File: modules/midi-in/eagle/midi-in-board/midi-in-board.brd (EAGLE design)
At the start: 101.6 x 63.5 mm, 28 parts, among them IC1 LM358N, X1 POWER IN, X2 MIDI IN, X3 MIDI THRU, X4 CHANNEL SELECT SW, X5 22-23-2051, X6 POWER OUT CV

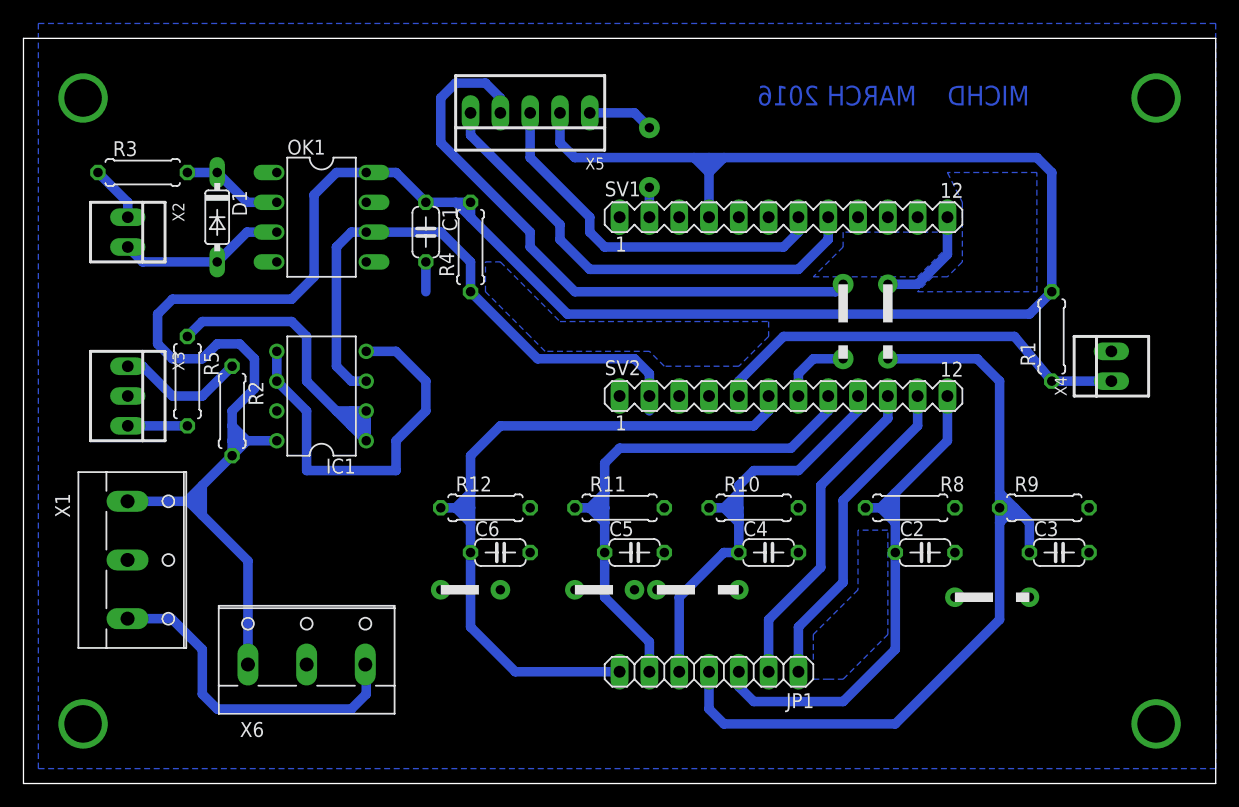
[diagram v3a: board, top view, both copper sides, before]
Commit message: Resize boards to be 10cm wide exactly
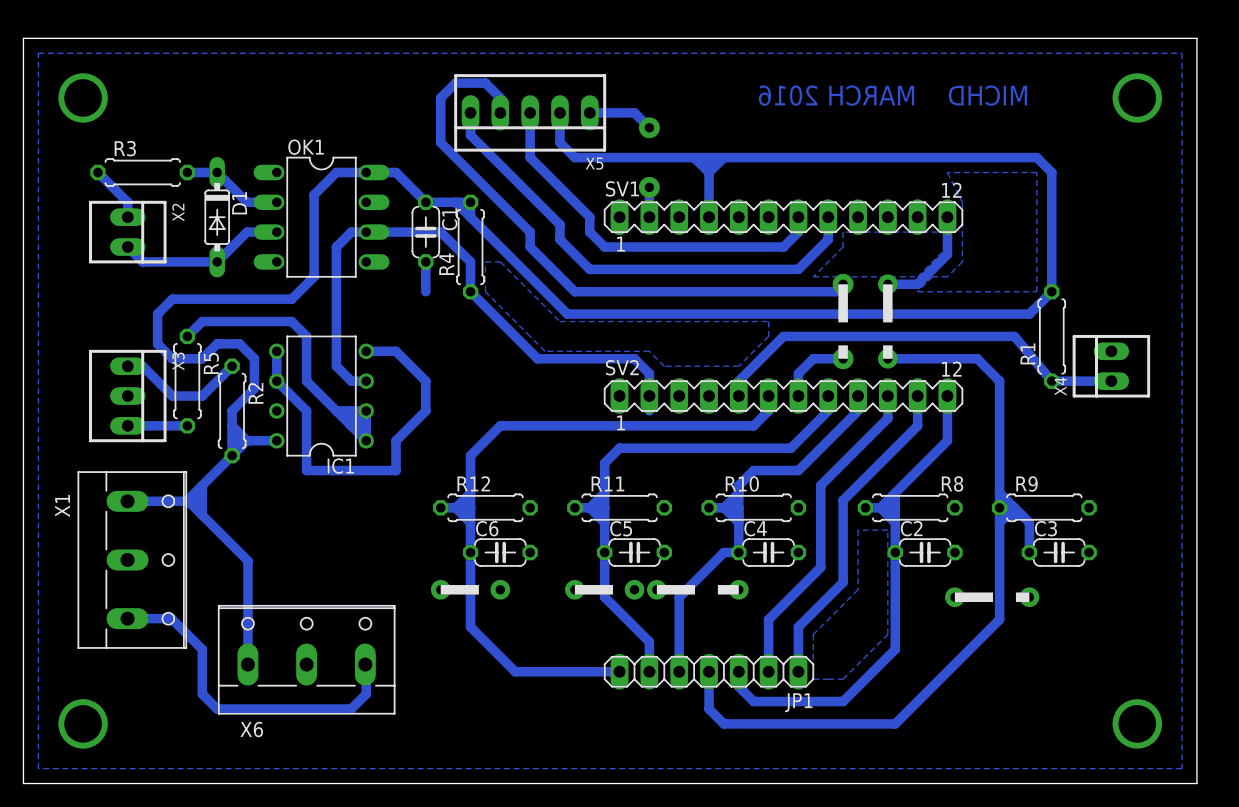
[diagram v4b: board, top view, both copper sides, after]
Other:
- board size 101.6 x 63.5 mm -> 100 x 63.5 mm
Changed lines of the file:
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@@
 <setting verticaltext="up"/>
 </settings>
-<grid distance="0.05" unitdist="inch" unit="mm" style="lines" multiple="1" display="no" altdistance="0.025" altunitdist="inch" altunit="inch"/>
+<grid distance="0.05" unitdist="inch" unit="mm" style="lines" multiple="1" display="yes" altdistance="0.025" altunitdist="inch" altunit="inch"/>
 <layers>
 <layer number="1" name="Top" color="4" fill="1" visible="yes" active="yes"/>
@@
 <board>
 <plain>
-<wire x1="0" y1="0" x2="101.6" y2="0" width="0" layer="20"/>
-<wire x1="101.6" y1="0" x2="101.6" y2="63.5" width="0" layer="20"/>
-<wire x1="101.6" y1="63.5" x2="0" y2="63.5" width="0" layer="20"/>
+<wire x1="0" y1="0" x2="100" y2="0" width="0" layer="20"/>
+<wire x1="100" y1="0" x2="100" y2="63.5" width="0" layer="20"/>
+<wire x1="100" y1="63.5" x2="0" y2="63.5" width="0" layer="20"/>
 <wire x1="0" y1="63.5" x2="0" y2="0" width="0" layer="20"/>
 <wire x1="53.34" y1="55.88" x2="53.34" y2="50.8" width="0.8128" layer="22" style="shortdash"/>
@@
 <contactref element="X1" pad="2"/>
 <polygon width="0.8128" layer="16" isolate="1.27">
-<vertex x="1.27" y="64.77"/>
-<vertex x="101.6" y="64.77"/>
-<vertex x="101.6" y="1.27"/>
+<vertex x="1.27" y="62.23"/>
+<vertex x="98.73" y="62.23"/>
+<vertex x="98.73" y="1.27"/>
 <vertex x="1.27" y="1.27"/>
 </polygon>
@@
 <signal name="N$50">
 <via x="5.08" y="58.42" extent="1-16" drill="3.2" diameter="4"/>
-<via x="96.52" y="58.42" extent="1-16" drill="3.2" diameter="4"/>
+<via x="94.92" y="58.42" extent="1-16" drill="3.2" diameter="4"/>
 <via x="5.08" y="5.08" extent="1-16" drill="3.2" diameter="4"/>
-<via x="96.52" y="5.08" extent="1-16" drill="3.2" diameter="4"/>
-<wire x1="96.52" y1="5.08" x2="96.52" y2="58.42" width="0" layer="19" extent="1-1"/>
-<wire x1="5.08" y1="58.42" x2="96.52" y2="58.42" width="0" layer="19" extent="1-1"/>
+<via x="94.92" y="5.08" extent="1-16" drill="3.2" diameter="4"/>
+<wire x1="94.92" y1="5.08" x2="94.92" y2="58.42" width="0" layer="19" extent="1-1"/>
+<wire x1="5.08" y1="58.42" x2="94.92" y2="58.42" width="0" layer="19" extent="1-1"/>
 <wire x1="5.08" y1="5.08" x2="5.08" y2="58.42" width="0" layer="19" extent="1-1"/>
 </signal>

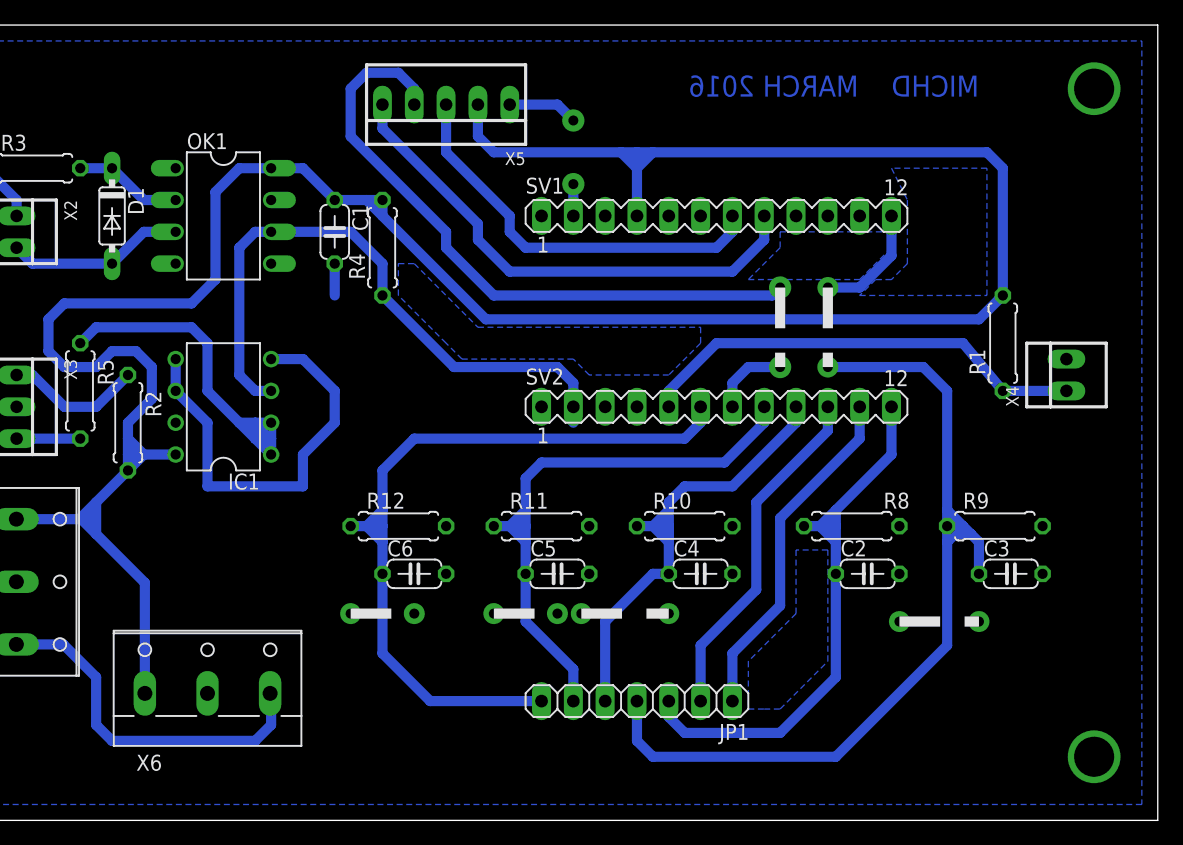
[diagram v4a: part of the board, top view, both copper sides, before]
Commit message: Redesign of MIDI in board, now with DAC.
Remapped the names of DAC channels, for more straightforward PCB routing.
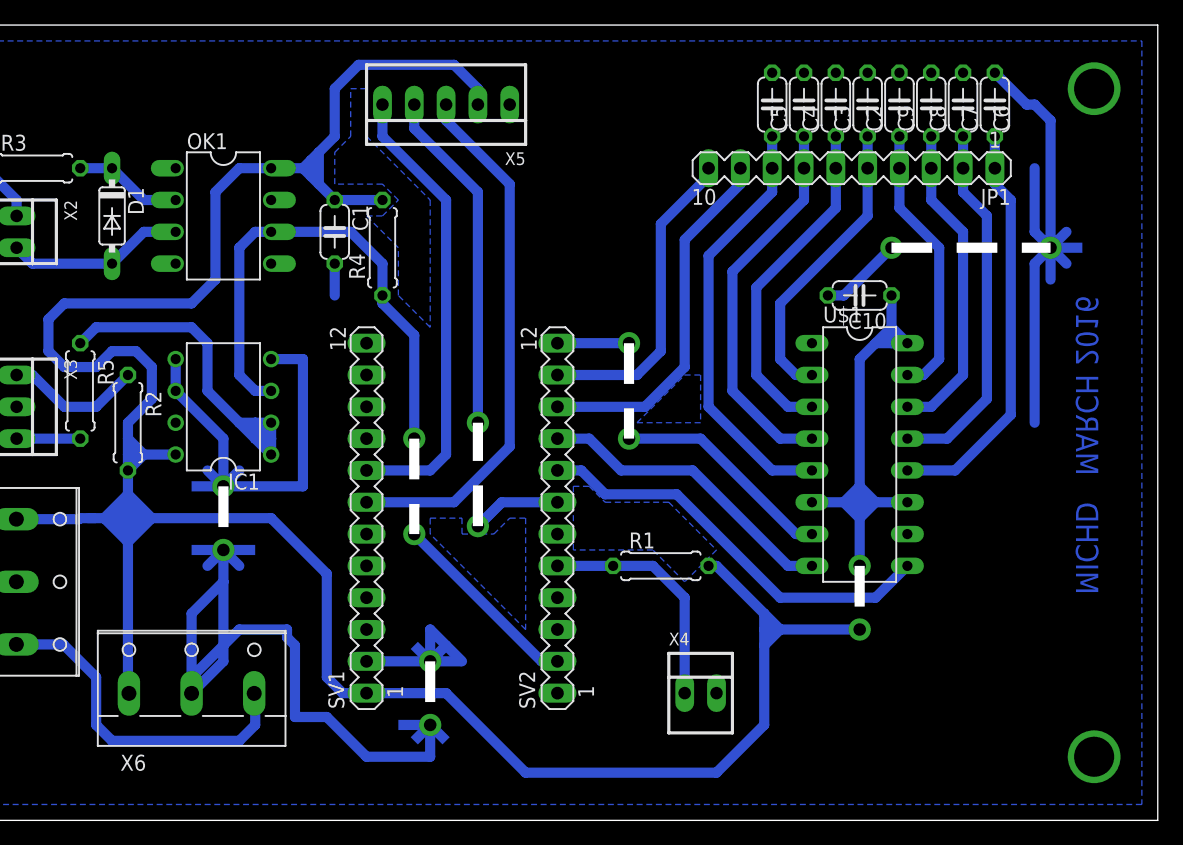
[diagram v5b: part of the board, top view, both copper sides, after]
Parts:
- removed R10, R11, R12, R8, R9: 10K, rcl:0207/7
- added C10, C7, C8, C9: 100n, rcl:C050-024X044
- added U$1: LTC1660, LTC1660:DIL16
- JP1: device pinhead:1X07 -> con-lstb:MA10-1
- moved C6 59.6 mm to (87.0, 57.1), turned to 90 degrees
- moved JP1 45.9 mm to (75.6, 52.1)
- moved C5 41.2 mm to (69.2, 57.1), turned to 90 degrees
- moved C3 40.0 mm to (74.3, 57.1), turned to 90 degrees
- moved X4 38.7 mm to (63.5, 10.2), turned to 0 degrees
- moved C4 38.4 mm to (71.8, 57.1), turned to 90 degrees
- moved C2 37.5 mm to (76.8, 57.1), turned to 90 degrees
- moved SV1 36.9 mm to (36.8, 24.1), turned to 90 degrees
- moved R1 32.6 mm to (60.3, 20.3), turned to 0 degrees
- moved SV2 15.5 mm to (52.1, 24.1), turned to 90 degrees
- moved X6 1.27 mm to (22.9, 11.4)
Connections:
- removed net N$13: C2.1, JP1.3, R8.1, SV2.12
- removed net N$18: C6.1, JP1.7, R12.1, SV2.6
- removed net N$20: C3.1, JP1.4, R9.1, SV1.12
- new net N$22: C2.1, JP1.5, U$1.2
- new net N$23: SV2.12, U$1.7
- new net N$27: C3.1, JP1.6, U$1.3
- new net N$31: C6.1, JP1.1, U$1.12
- new net N$33: C4.1, JP1.7, U$1.4
- new net N$34: C5.1, JP1.8, U$1.5
- new net N$36: C7.1, JP1.2, U$1.13
- new net N$37: C8.1, JP1.3, U$1.14
- new net N$38: C9.1, JP1.4, U$1.15
- net GND: now also C10.2, C7.2, C8.2, C9.2, U$1.1; no longer R10.2, R11.2, R12.2, R8.2, R9.2
- net N$11: now also JP1.10; no longer JP1.1
- net N$12: now also JP1.9; no longer JP1.2
- net N$16: now also U$1.8; no longer C4.1, JP1.5, R10.1
- net N$17: now also U$1.9; no longer C5.1, JP1.6, R11.1
- net VCC: now also C10.1, SV1.1, U$1.11, U$1.16, U$1.6; no longer SV1.4
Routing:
- net GND: track 44.3 -> 178.0 mm, vias 10 -> 5
- net N$20: track 82.6 -> 0.00 mm, vias 2 -> 1
- net N$18: track 63.3 -> 0.00 mm, vias 0 -> 1
- net VCC: track 217.2 -> 271.3 mm, vias 0 -> 1
- net N$13: track 46.5 -> 0.00 mm, vias 0 -> 1
- net N$34: track 0.00 -> 34.1 mm
- net N$31: track 0.00 -> 32.8 mm
- net N$33: track 0.00 -> 30.6 mm
- net N$36: track 0.00 -> 29.4 mm
- net N$27: track 0.00 -> 27.2 mm
- net N$37: track 0.00 -> 25.6 mm
- net N$22: track 0.00 -> 23.7 mm
- net N$23: track 0.00 -> 23.5 mm
- net N$38: track 0.00 -> 22.2 mm
- net N$24: track 58.0 -> 37.3 mm, vias 0 -> 2
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- added copper zone on layer 16, net N$28
- added copper zone on layer 16, net N$29
- added copper zone on layer 16, net N$32
- removed copper zone on layer 16, net N$15
- removed copper zone on layer 16, net N$19
- removed copper zone on layer 16, net N$8
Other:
- outline, holes or cut-outs redrawn
